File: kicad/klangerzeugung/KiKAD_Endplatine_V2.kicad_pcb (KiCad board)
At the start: 2 copper layers, 100 x 80 mm, 65 parts, among them J1 Conn_02x08_Odd_Even, Q1 Q_NPN_BEC, Q2 Q_NPN_BEC, Q3 Q_NPN_BEC, Q4 Q_NPN_BEC, U1 NE555P, U2 TL074

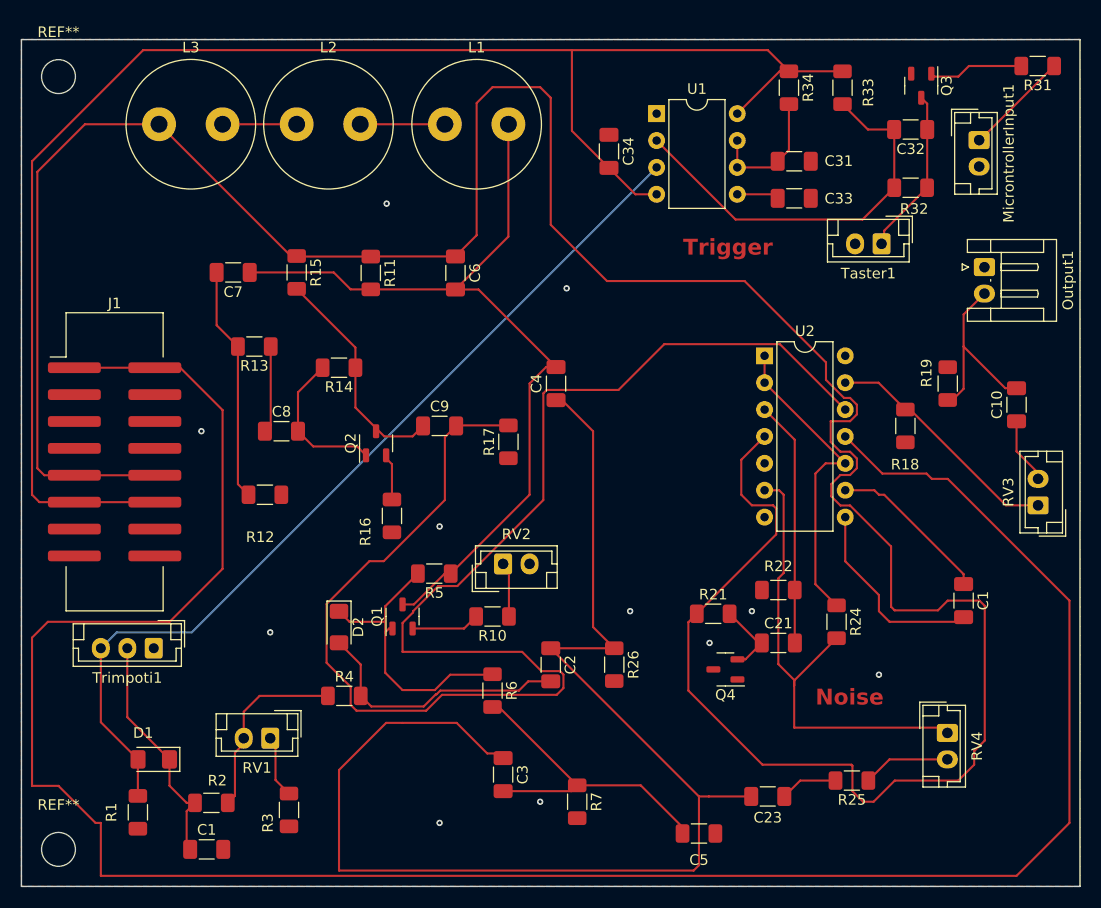
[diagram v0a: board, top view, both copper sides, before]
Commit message: Schaltungsplan Update
Massebezug hergestellt, update zu Footprints
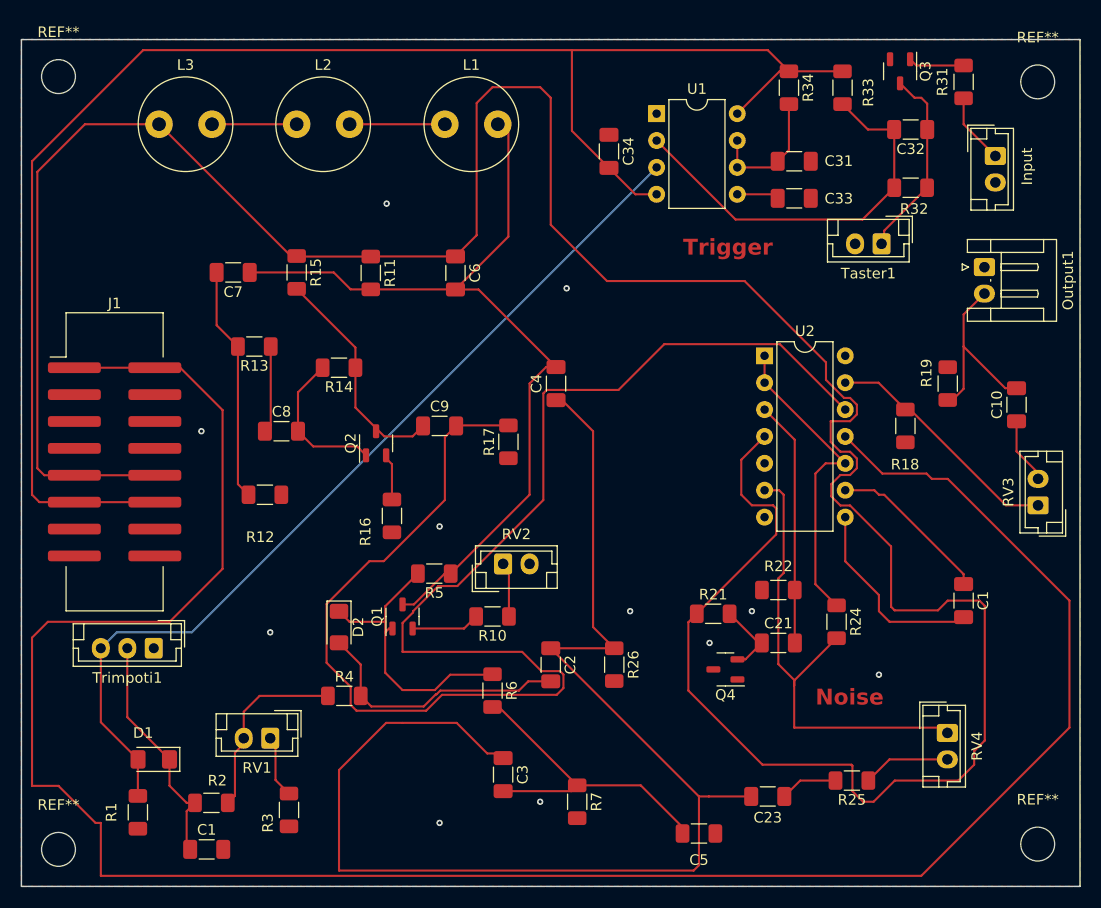
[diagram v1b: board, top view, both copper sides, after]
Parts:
- added REF**: MountingHole_3.2mm_M3, MountingHole:MountingHole_3.2mm_M3, F.Cu at (196.0, 111.0)
- added REF**: MountingHole_3.2mm_M3, MountingHole:MountingHole_3.2mm_M3, F.Cu at (196.0, 39.0)
- L1, L2, L3: footprint Inductor_THT:L_Radial_D12.0mm_P6.00mm_Murata_1900R -> Inductor_THT:L_Radial_D8.7mm_P5.00mm_Fastron_07HCP
- moved R31 7.16 mm to (189.0, 39.0), turned to 90 degrees
- moved Q3 2.42 mm to (183.0, 38.0)
- moved Input 2.14 mm to (192.0, 46.0)
- renumbered MicrontrollerInput1 to Input
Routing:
- net -12V: track 220.5 -> 215.2 mm
- net Net-(Q3-B): track 9.03 -> 5.29 mm
- net Net-(MicrontrollerInput1-Pin_1): track 9.98 -> 6.69 mm
- net Net-(Q3-C): track 15.9 -> 18.4 mm

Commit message: Update 2 zu Platinen
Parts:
- Output1: footprint Connector_JST:JST_EH_S2B-EH_1x02_P2.50mm_Horizontal -> Connector_JST:JST_EH_B2B-EH-A_1x02_P2.50mm_Vertical
- moved REF** 0.71 mm to (196.5, 111.5)
- moved REF** 0.71 mm to (196.5, 38.5)
- renumbered Input to MicrontrollerInput1

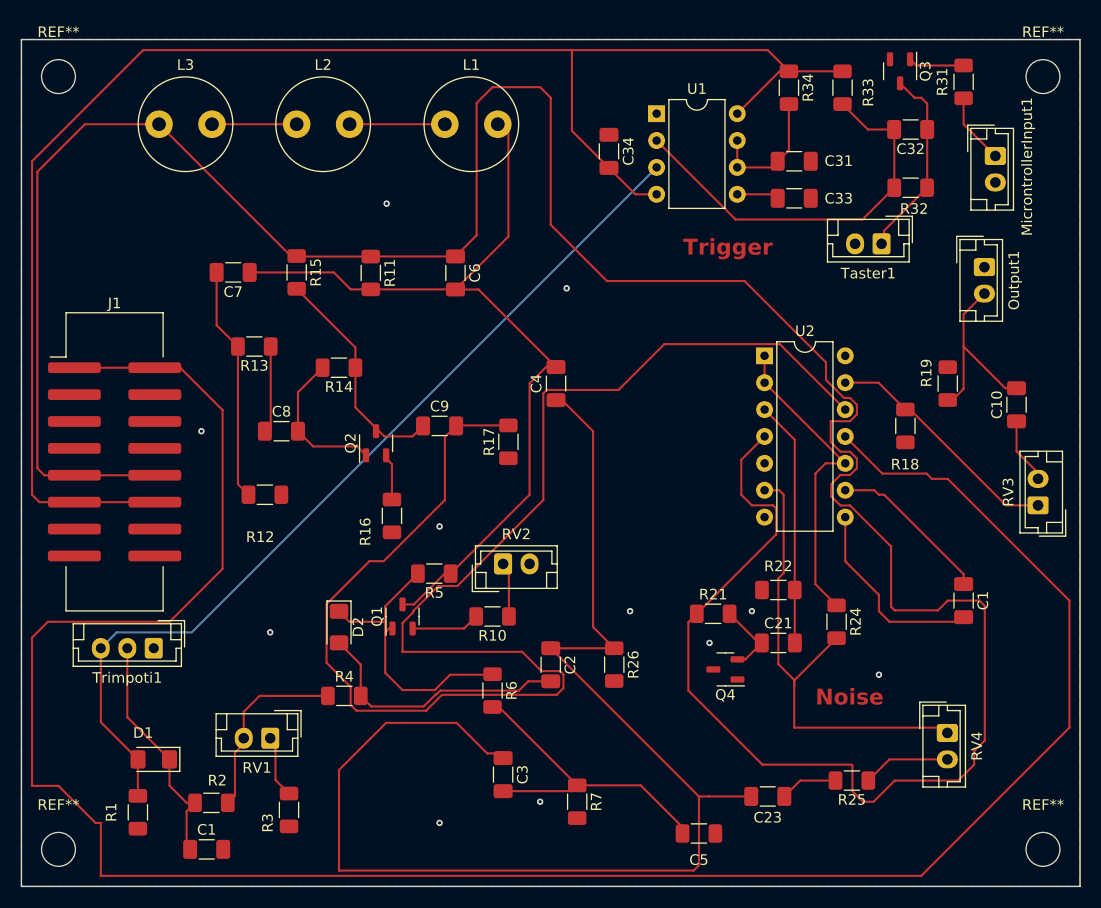
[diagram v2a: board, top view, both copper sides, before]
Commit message: Neues Platinendesign
Neues Platinendesign
- Angenehmeres Design
- Drahtbrücken in Schaltung inbegriffen
- Bessere Footprints
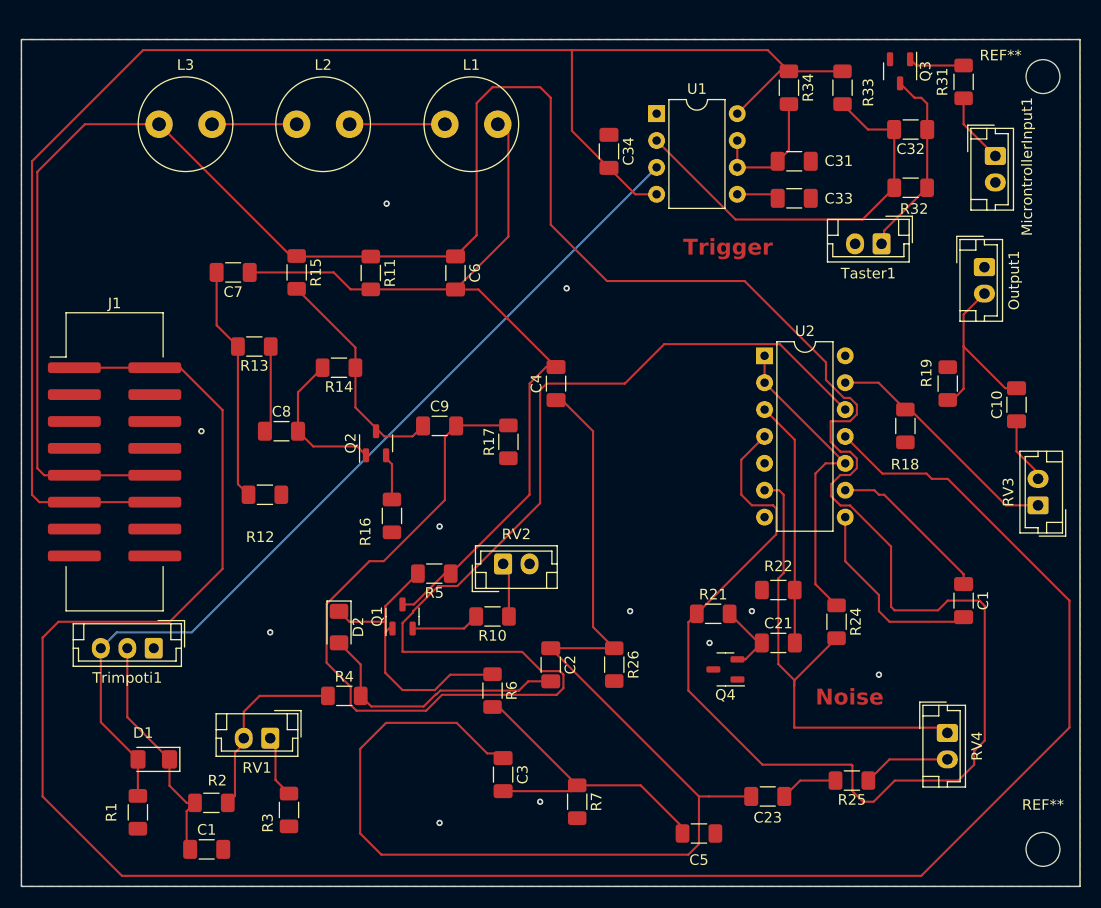
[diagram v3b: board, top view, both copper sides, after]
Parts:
- removed the REF** at (103.5, 111.5)
- removed the REF** at (103.5, 38.5)
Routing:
- net Net-(C2-Pad1): track 125.7 -> 118.4 mm
- net -12V: track 215.2 -> 210.9 mm
